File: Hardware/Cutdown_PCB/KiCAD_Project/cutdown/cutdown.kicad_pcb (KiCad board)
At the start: 4 copper layers, 24.1 x 60.3 mm, 24 parts, among them J1 Nichrome Wire, Q1 MMBT3904, U1 Particle, U2 BMP388, U3 ublox_SAM-M8Q

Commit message: Cutdown PCB Rev 1.0 Complete.
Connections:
- J1 pad 3: Net-(J1-Pad1) -> EXT_CUTDOWN
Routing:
- net EXT_CUTDOWN: track 11.2 -> 81.1 mm
- net Net-(J1-Pad1): track 9.32 -> 3.20 mm
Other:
- board text added: "Balloon Cutdown Module Rev. 1.0 November 2019 P/N 3-0000018"
- board text added: "Ext"
- board text removed: "Leeman Geophysical LLC Balloon Cutdown Module Rev. 1.0 November 2019 P/N 3-0000018"
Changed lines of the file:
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@@
     (thickness 1.6)
     (drawings 9)
-    (tracks 218)
+    (tracks 223)
     (zones 0)
     (modules 24)
@@
       (net 2 GND))
     (pad 3 thru_hole oval (at 0 5.08 90) (size 1.7 1.7) (drill 1) (layers *.Cu *.Mask)
-      (net 5 "Net-(J1-Pad1)"))
+      (net 16 EXT_CUTDOWN))
     (pad 2 thru_hole oval (at 0 2.54 90) (size 1.7 1.7) (drill 1) (layers *.Cu *.Mask)
       (net 2 GND))
@@
     )
   )
-  (gr_text "Leeman Geophysical LLC\nBalloon Cutdown Module\nRev. 1.0 November 2019\nP/N 3-0000018" (at 193.294 93.472) (layer B.SilkS)
+  (gr_text "Balloon Cutdown Module\nRev. 1.0 November 2019\nP/N 3-0000018" (at 193.294 93.472) (layer B.SilkS)
     (effects (font (size 0.762 0.762) (thickness 0.1905)) (justify mirror))
   )
@@
     (effects (font (size 1.5 1.5) (thickness 0.3)) (justify mirror))
   )
-  (gr_text Cut (at 192.659 101.473 90) (layer B.SilkS)
+  (gr_text Ext (at 192.659 101.473 90) (layer B.SilkS)
     (effects (font (size 1.5 1.5) (thickness 0.3)) (justify mirror))
   )
@@
   (segment (start 191.6 76.03) (end 191.643 76.073) (width 0.1524) (layer B.Cu) (net 3))
   (segment (start 195.496 65.278) (end 193.675 65.278) (width 0.3048) (layer B.Cu) (net 3) (status 10))
-  (segment (start 193.675 64.051) (end 193.718 64.008) (width 0.3048) (layer F.Cu) (net 10) (status 30))
   (via (at 198.501 49.022) (size 0.508) (drill 0.254) (layers F.Cu B.Cu) (net 3))
   (segment (start 197.485 49.573) (end 197.95 49.573) (width 0.3048) (layer B.Cu) (net 3) (status 10))
@@
   (segment (start 195.496 65.278) (end 195.496 65.405) (width 0.3048) (layer B.Cu) (net 3) (status 30))
   (via (at 200.53299 88.4174) (size 0.508) (drill 0.254) (layers F.Cu B.Cu) (net 3))
-  (segment (start 199.771 87.333) (end 199.771 87.65541) (width 0.1524) (layer F.Cu) (net 3))
-  (segment (start 199.771 87.65541) (end 200.53299 88.4174) (width 0.1524) (layer F.Cu) (net 3))
+  (segment (start 199.771 87.333) (end 199.771 87.65541) (width 0.1524) (layer F.Cu) (net 3) (status 30))
+  (segment (start 199.771 87.65541) (end 200.53299 88.4174) (width 0.1524) (layer F.Cu) (net 3) (status 10))
   (via (at 194.183 83.82) (size 0.508) (drill 0.254) (layers F.Cu B.Cu) (net 3))
-  (segment (start 195.496 83.82) (end 194.183 83.82) (width 0.1524) (layer B.Cu) (net 3))
+  (segment (start 195.496 83.82) (end 194.183 83.82) (width 0.1524) (layer B.Cu) (net 3) (status 10))
   (segment (start 196.614001 57.843001) (end 196.614001 61.195999) (width 0.508) (layer B.Cu) (net 4))
   (segment (start 193.508 54.737) (end 196.614001 57.843001) (width 0.508) (layer B.Cu) (net 4) (status 10))
@@
   (segment (start 193.508 54.613) (end 192.108 53.213) (width 0.508) (layer B.Cu) (net 4) (status 30))
   (segment (start 193.508 54.737) (end 193.508 54.613) (width 0.508) (layer B.Cu) (net 4) (status 30))
-  (segment (start 188.835401 105.042599) (end 187.579 106.299) (width 0.508) (layer B.Cu) (net 5) (status 20))
-  (segment (start 191.402599 105.042599) (end 188.835401 105.042599) (width 0.508) (layer B.Cu) (net 5))
-  (segment (start 192.659 106.299) (end 191.402599 105.042599) (width 0.508) (layer B.Cu) (net 5) (status 10))
   (segment (start 185.336 106.299) (end 184.658 105.621) (width 0.508) (layer F.Cu) (net 5) (status 20))
   (segment (start 187.579 106.299) (end 185.336 106.299) (width 0.508) (layer F.Cu) (net 5) (status 10))
@@
   (segment (start 202.819 55.9816) (end 201.4474 54.61) (width 0.1524) (layer F.Cu) (net 9) (status 20))
   (segment (start 202.819 82.931) (end 202.819 55.9816) (width 0.1524) (layer F.Cu) (net 9))
+  (segment (start 193.675 64.051) (end 193.718 64.008) (width 0.3048) (layer F.Cu) (net 10) (status 30))
   (segment (start 196.700881 63.035601) (end 198.501 61.235482) (width 0.1524) (layer F.Cu) (net 10))
   (segment (start 194.087999 63.035601) (end 196.700881 63.035601) (width 0.1524) (layer F.Cu) (net 10))
@@
   (segment (start 199.009 66.718) (end 198.966 66.675) (width 0.1524) (layer B.Cu) (net 12) (status 30))
   (segment (start 199.009 68.58) (end 199.009 66.718) (width 0.1524) (layer B.Cu) (net 12) (status 20))
-  (segment (start 198.25 86.864) (end 198.759 86.864) (width 0.1524) (layer B.Cu) (net 12))
+  (segment (start 198.25 86.864) (end 198.759 86.864) (width 0.1524) (layer B.Cu) (net 12) (status 10))
   (segment (start 198.759 86.864) (end 199.59318 86.02982) (width 0.1524) (layer B.Cu) (net 12))
   (segment (start 199.59318 69.16418) (end 199.009 68.58) (width 0.1524) (layer B.Cu) (net 12))
@@
   (segment (start 201.1426 59.69) (end 201.295 59.69) (width 0.1524) (layer B.Cu) (net 16) (status 30))
   (segment (start 197.485 56.0324) (end 201.1426 59.69) (width 0.1524) (layer B.Cu) (net 16) (status 20))
-  (segment (start 197.485 51.773) (end 197.485 56.0324) (width 0.1524) (layer B.Cu) (net 16) (status 10))
+  (segment (start 189.125119 52.534399) (end 196.298399 52.534399) (width 0.1524) (layer B.Cu) (net 16))
+  (segment (start 185.318399 56.341119) (end 189.125119 52.534399) (width 0.1524) (layer B.Cu) (net 16))
+  (segment (start 185.318399 103.482649) (end 185.318399 56.341119) (width 0.1524) (layer B.Cu) (net 16))
+  (segment (start 185.696351 103.860601) (end 185.318399 103.482649) (width 0.1524) (layer B.Cu) (net 16))
+  (segment (start 190.220601 103.860601) (end 185.696351 103.860601) (width 0.1524) (layer B.Cu) (net 16))
+  (segment (start 196.298399 52.534399) (end 197.485 53.721) (width 0.1524) (layer B.Cu) (net 16))
+  (segment (start 192.659 106.299) (end 190.220601 103.860601) (width 0.1524) (layer B.Cu) (net 16))
+  (segment (start 197.485 53.721) (end 197.485 56.0324) (width 0.1524) (layer B.Cu) (net 16))
+  (segment (start 197.485 51.773) (end 197.485 53.721) (width 0.1524) (layer B.Cu) (net 16))
   (segment (start 200.6926 85.133) (end 199.771 85.133) (width 0.1524) (layer F.Cu) (net 17) (status 20))
   (segment (start 201.295 85.133) (end 200.6926 85.133) (width 0.1524) (layer F.Cu) (net 17) (status 10))
@@
   (segment (start 198.501 84.836) (end 198.501 85.333) (width 0.1524) (layer B.Cu) (net 17))
   (segment (start 198.983601 84.355201) (end 198.983601 86.004399) (width 0.1524) (layer B.Cu) (net 18))
-  (segment (start 197.696 83.82) (end 198.4484 83.82) (width 0.1524) (layer B.Cu) (net 18))
+  (segment (start 197.696 83.82) (end 198.4484 83.82) (width 0.1524) (layer B.Cu) (net 18) (status 10))
   (segment (start 198.4484 83.82) (end 198.983601 84.355201) (width 0.1524) (layer B.Cu) (net 18))
-  (segment (start 198.624 86.364) (end 198.25 86.364) (width 0.1524) (layer B.Cu) (net 18))
+  (segment (start 198.624 86.364) (end 198.25 86.364) (width 0.1524) (layer B.Cu) (net 18) (status 20))
   (segment (start 198.983601 86.004399) (end 198.624 86.364) (width 0.1524) (layer B.Cu) (net 18))
   (zone (net 3) (net_name +3V3) (layer In1.Cu) (hatch edge 0.508)

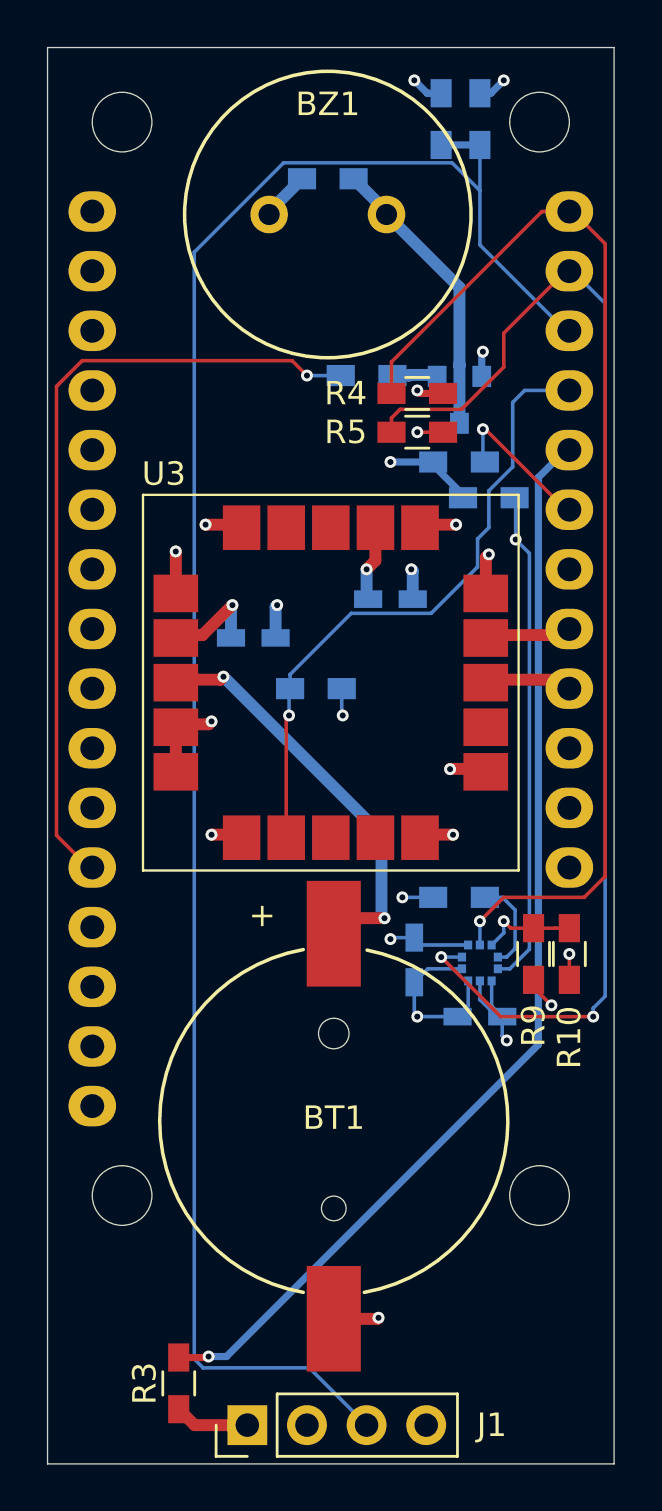
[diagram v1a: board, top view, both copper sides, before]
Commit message: Fix GPS connection to particle.
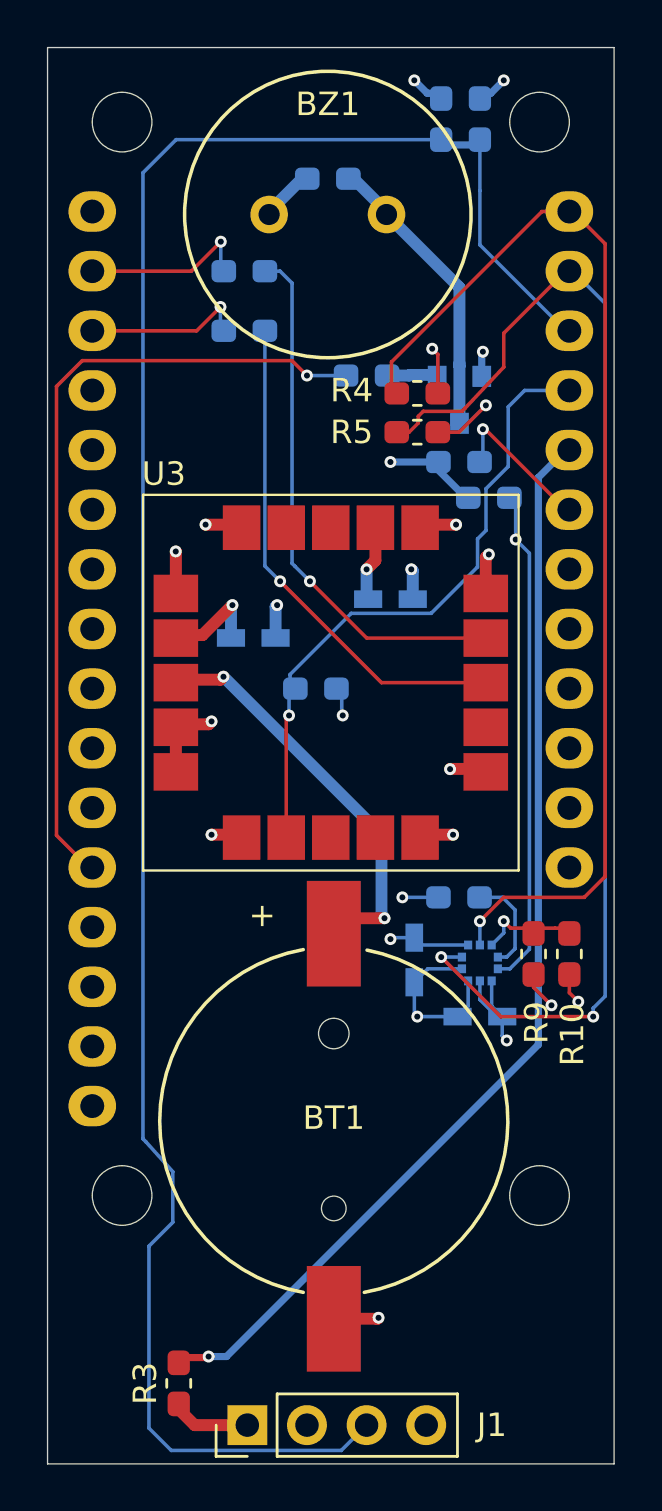
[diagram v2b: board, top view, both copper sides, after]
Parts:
- added R14: 0R0, Resistor_SMD:R_0603_1608Metric_Pad1.05x0.95mm_HandSolder, B.Cu at (187.5, 59.7)
- added R15: 0R0, Resistor_SMD:R_0603_1608Metric_Pad1.05x0.95mm_HandSolder, B.Cu at (187.5, 57.1)
- R1, R10, R11, R12, R13, R2, R3, R4, R5, R6, R7, R8: footprint Resistors_SMD:R_0603_HandSoldering -> Resistor_SMD:R_0603_1608Metric_Pad1.05x0.95mm_HandSolder
- R9: value 10k -> NP; footprint Resistors_SMD:R_0603_HandSoldering -> Resistor_SMD:R_0603_1608Metric_Pad1.05x0.95mm_HandSolder
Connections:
- U1 pad 1: (no net) -> Net-(U1-Pad1)
- U1 pad 10: (no net) -> Net-(U1-Pad10)
- U1 pad 11: (no net) -> Net-(U1-Pad11)
- U1 pad 12: (no net) -> Net-(U1-Pad12)
- U1 pad 13: (no net) -> Net-(U1-Pad13)
- U1 pad 14: (no net) -> Net-(R14-Pad1)
- U1 pad 15: (no net) -> Net-(R15-Pad1)
- U1 pad 16: (no net) -> Net-(U1-Pad16)
- U1 pad 17: (no net) -> Net-(U1-Pad17)
- U1 pad 18: (no net) -> Net-(U1-Pad18)
- U1 pad 19: (no net) -> Net-(U1-Pad19)
- U1 pad 20: GPS_TX -> Net-(U1-Pad20)
- U1 pad 21: GPS_RX -> Net-(U1-Pad21)
- U1 pad 3: (no net) -> Net-(U1-Pad3)
- U1 pad 6: (no net) -> Net-(U1-Pad6)
- U1 pad 7: (no net) -> Net-(U1-Pad7)
- U1 pad 8: (no net) -> Net-(U1-Pad8)
- U1 pad 9: (no net) -> Net-(U1-Pad9)
- U3 pad 12: (no net) -> Net-(U3-Pad12)
- U3 pad 18: (no net) -> Net-(U3-Pad18)
- U3 pad 19: (no net) -> Net-(U3-Pad19)
- U3 pad 8: (no net) -> Net-(U3-Pad8)
- U3 pad 9: (no net) -> Net-(U3-Pad9)
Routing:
- net GPS_RX: track 3.67 -> 22.9 mm, vias 0 -> 1
- net GPS_TX: track 3.72 -> 21.5 mm, vias 0 -> 1
- net EXT_CUTDOWN: track 81.1 -> 89.0 mm
- net Net-(R15-Pad1): track 0.00 -> 7.30 mm, vias 0 -> 1
- net Net-(R14-Pad1): track 0.00 -> 6.96 mm, vias 0 -> 1
- net +3V3: track 27.9 -> 30.2 mm
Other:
- board text added: "Balloon Cutdown Module Rev. 2.0 April 2020 P/N 3-0000028"
- board text removed: "Balloon Cutdown Module Rev. 1.0 November 2019 P/N 3-0000018"
